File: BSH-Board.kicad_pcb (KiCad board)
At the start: 2 copper layers, 20 x 30 mm, 47 parts, among them J1 667101210103, J2 MICRO QTZB5.0, SW1 TS-3025-B-C-B, SW2 TS-3025-B-C-B, U1 ESP32-C6-MINI-1-N4, U2 AP63203WU, U3 NCP715SQ50T2G, U4 TXS0102DQER

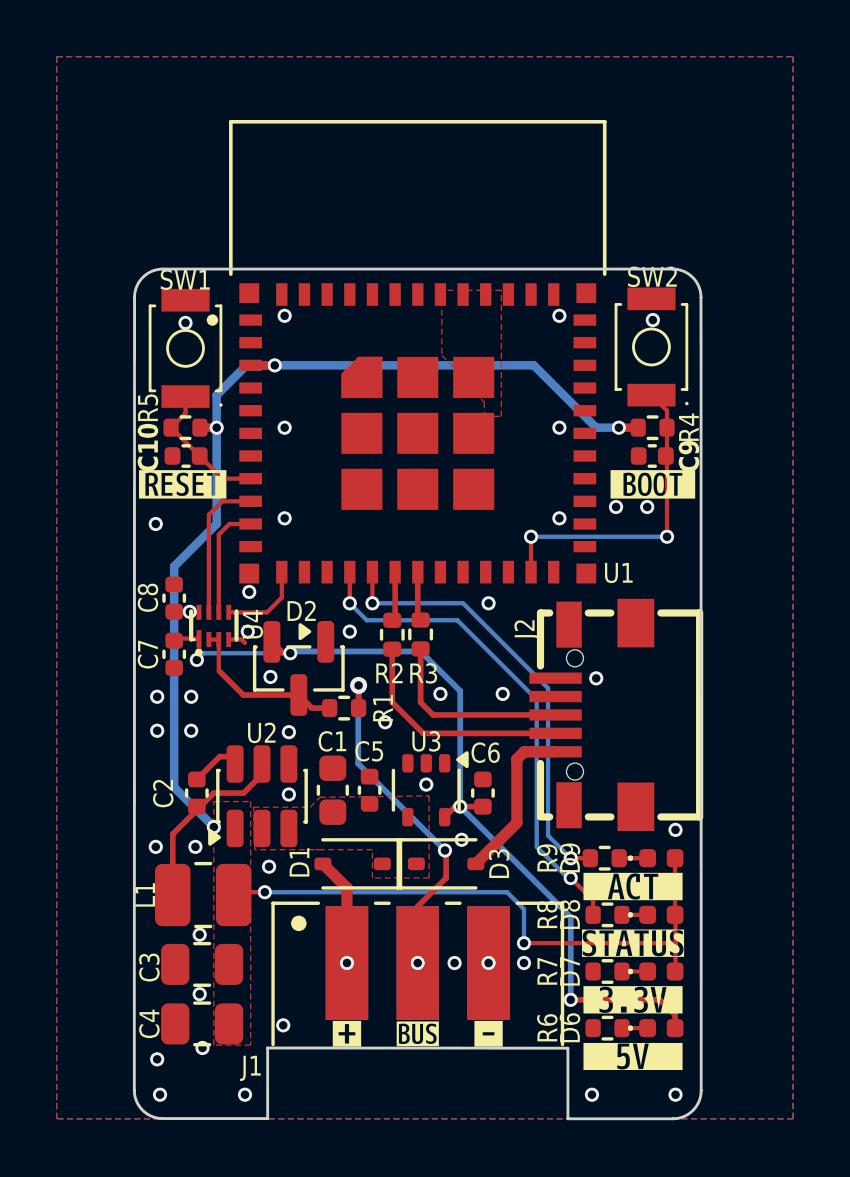
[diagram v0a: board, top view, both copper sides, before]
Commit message: Fix TXS0102DQER bug
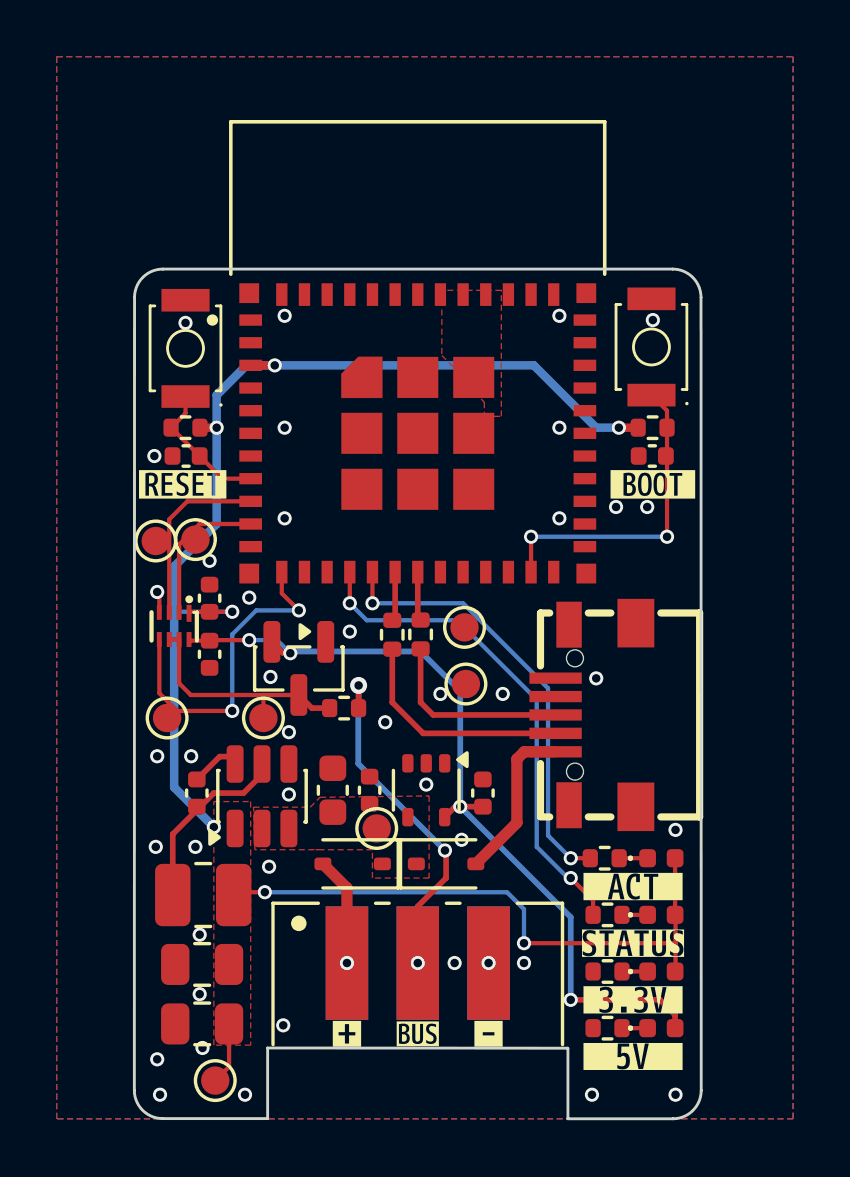
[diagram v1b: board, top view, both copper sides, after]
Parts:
- added TP1: TestPoint, TestPoint:TestPoint_Pad_D1.0mm, F.Cu at (113.2, 76.8)
- added TP2: TestPoint, TestPoint:TestPoint_Pad_D1.0mm, F.Cu at (116.5, 76.8)
- added TP3: TestPoint, TestPoint:TestPoint_Pad_D1.0mm, F.Cu at (114.2, 70.5)
- added TP4: TestPoint, TestPoint:TestPoint_Pad_D1.0mm, F.Cu at (112.8, 70.6)
- added TP5: TestPoint, TestPoint:TestPoint_Pad_D1.0mm, F.Cu at (123.7, 73.7)
- added TP6: TestPoint, TestPoint:TestPoint_Pad_D1.0mm, F.Cu at (120.5, 80.8)
- added TP7: TestPoint, TestPoint:TestPoint_Pad_D1.0mm, F.Cu at (114.8, 89.7)
- added TP8: TestPoint, TestPoint:TestPoint_Pad_D1.0mm, F.Cu at (123.7, 75.7)
- moved U4 1.40 mm to (113.4, 73.6), turned to 180 degrees
- moved C7 1.25 mm to (114.7, 74.6)
- moved C8 1.25 mm to (114.7, 72.6)
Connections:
- U4 pad 1: +5V -> +3.3V
- U4 pad 2: D-BUS -> DBUS-TX
- U4 pad 3: D-BUS -> DBUS-RX
- U4 pad 6: DBUS-TX -> D-BUS
- U4 pad 7: DBUS-RX -> D-BUS
- U4 pad 8: +3.3V -> +5V
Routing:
- net DBUS-ENABLE: track 2.99 -> 11.7 mm, vias 0 -> 2
- net +3.3V: track 56.6 -> 61.0 mm
- net D-BUS: track 5.91 -> 8.38 mm
- net DBUS-RX: track 5.12 -> 6.42 mm
- net +5V: track 30.9 -> 29.6 mm
- net DBUS-TX: track 4.03 -> 5.22 mm
- net GND: track 0.62 -> 0.75 mm, vias 44 -> 42

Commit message: TXS0102 OE directly to 3.3v, all spare IOs to Testpoints
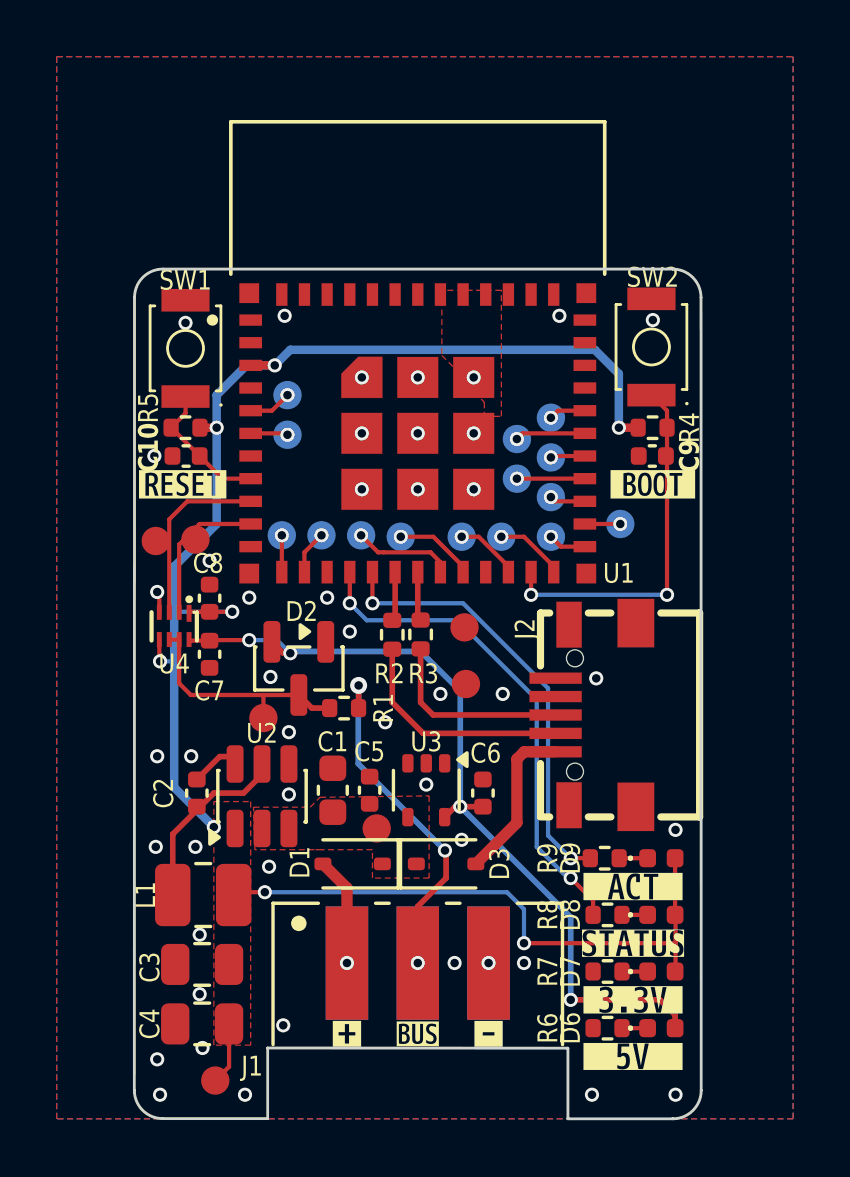
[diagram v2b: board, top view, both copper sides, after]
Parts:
- removed the TP1 at (113.2, 76.8)
- added TP10: TestPoint, Testpoints:TestPoint_Pad_D1.0mm, B.Cu at (117.4, 65.5)
- added TP11: TestPoint, Testpoints:TestPoint_Pad_D1.0mm, B.Cu at (117.4, 66.8)
- added TP12: TestPoint, Testpoints:TestPoint_Pad_D1.0mm, B.Cu at (123.5, 70.5)
- added TP13: TestPoint, Testpoints:TestPoint_Pad_D1.0mm, B.Cu at (120.0, 70.4)
- added TP14: TestPoint, Testpoints:TestPoint_Pad_D1.0mm, B.Cu at (121.4, 70.5)
- added TP15: TestPoint, Testpoints:TestPoint_Pad_D1.0mm, B.Cu at (125.0, 70.5)
- added TP16: TestPoint, Testpoints:TestPoint_Pad_D1.0mm, B.Cu at (126.7, 70.5)
- added TP17: TestPoint, Testpoints:TestPoint_Pad_D1.0mm, B.Cu at (129.2, 70.0)
- added TP18: TestPoint, Testpoints:TestPoint_Pad_D1.0mm, B.Cu at (126.7, 69.0)
- added TP19: TestPoint, Testpoints:TestPoint_Pad_D1.0mm, B.Cu at (125.5, 68.4)
- added TP20: TestPoint, Testpoints:TestPoint_Pad_D1.0mm, B.Cu at (126.7, 67.7)
- added TP21: TestPoint, Testpoints:TestPoint_Pad_D1.0mm, B.Cu at (126.7, 66.2)
- added TP22: TestPoint, Testpoints:TestPoint_Pad_D1.0mm, B.Cu at (125.5, 67.0)
- added TP8: TestPoint, Testpoints:TestPoint_Pad_D1.0mm, B.Cu at (117.2, 70.4)
- added TP9: TestPoint, Testpoints:TestPoint_Pad_D1.0mm, B.Cu at (118.6, 70.4)
- R6, R9: value 330 -> 510
- TP1: renamed from TP2; footprint TestPoint:TestPoint_Pad_D1.0mm -> Testpoints:TestPoint_Pad_D1.0mm
- TP2: renamed from TP3; footprint TestPoint:TestPoint_Pad_D1.0mm -> Testpoints:TestPoint_Pad_D1.0mm
- TP3: renamed from TP4; footprint TestPoint:TestPoint_Pad_D1.0mm -> Testpoints:TestPoint_Pad_D1.0mm
- TP4: renamed from TP5; footprint TestPoint:TestPoint_Pad_D1.0mm -> Testpoints:TestPoint_Pad_D1.0mm
- TP5: renamed from TP6; footprint TestPoint:TestPoint_Pad_D1.0mm -> Testpoints:TestPoint_Pad_D1.0mm
- TP6: renamed from TP7; footprint TestPoint:TestPoint_Pad_D1.0mm -> Testpoints:TestPoint_Pad_D1.0mm
- TP7: renamed from TP8; footprint TestPoint:TestPoint_Pad_D1.0mm -> Testpoints:TestPoint_Pad_D1.0mm
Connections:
- U1 pad 12: DBUS-ENABLE -> Net-(U1-IO0)
- U1 pad 13: unconnected-(U1-IO1-Pad13) -> Net-(U1-IO1)
- U1 pad 19: unconnected-(U1-IO14-Pad19) -> Net-(U1-IO14)
- U1 pad 20: unconnected-(U1-IO15-Pad20) -> Net-(U1-IO15)
- U1 pad 22: unconnected-(U1-IO8-Pad22) -> Net-(U1-IO8)
- U1 pad 24: unconnected-(U1-IO18-Pad24) -> Net-(U1-IO18)
- U1 pad 25: unconnected-(U1-IO19-Pad25) -> Net-(U1-IO19)
- U1 pad 26: unconnected-(U1-IO20-Pad26) -> Net-(U1-IO20)
- U1 pad 27: unconnected-(U1-IO21-Pad27) -> Net-(U1-IO21)
- U1 pad 28: unconnected-(U1-IO22-Pad28) -> Net-(U1-IO22)
- U1 pad 29: unconnected-(U1-IO23-Pad29) -> Net-(U1-IO23)
- U1 pad 30: unconnected-(U1-RXD0-Pad30) -> Net-(U1-RXD0)
- U1 pad 31: unconnected-(U1-TXD0-Pad31) -> Net-(U1-TXD0)
- U1 pad 5: unconnected-(U1-IO2-Pad5) -> Net-(U1-IO2)
- U1 pad 6: unconnected-(U1-IO3-Pad6) -> Net-(U1-IO3)
- U4 pad 5: DBUS-ENABLE -> +3.3V
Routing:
- net DBUS-ENABLE: track 11.7 -> 0.00 mm, vias 2 -> 0
- net Net-(U1-IO14): track 0.00 -> 3.54 mm, vias 0 -> 1
- net +3.3V: track 61.0 -> 63.9 mm, vias 7 -> 8
- net Net-(U1-IO15): track 0.00 -> 2.83 mm, vias 0 -> 1
- net Net-(U1-IO18): track 0.00 -> 2.48 mm, vias 0 -> 1
- net Net-(U1-RXD0): track 0.00 -> 2.48 mm, vias 0 -> 1
- net Net-(U1-IO22): track 0.00 -> 2.40 mm, vias 0 -> 1
- net Net-(U1-IO8): track 0.00 -> 2.28 mm, vias 0 -> 1
- net BOOT: track 11.3 -> 12.9 mm
- net Net-(U1-IO1): track 0.00 -> 1.55 mm, vias 0 -> 1
- net Net-(U1-IO2): track 0.00 -> 1.53 mm, vias 0 -> 1
- net Net-(U1-IO19): track 0.00 -> 1.34 mm, vias 0 -> 1
- net Net-(U1-IO3): track 0.00 -> 1.32 mm, vias 0 -> 1
- net Net-(U1-TXD0): track 0.00 -> 1.30 mm, vias 0 -> 1
- net Net-(U1-IO0): track 0.00 -> 1.30 mm, vias 0 -> 1
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
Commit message: Removed bottom pads of RAST connector
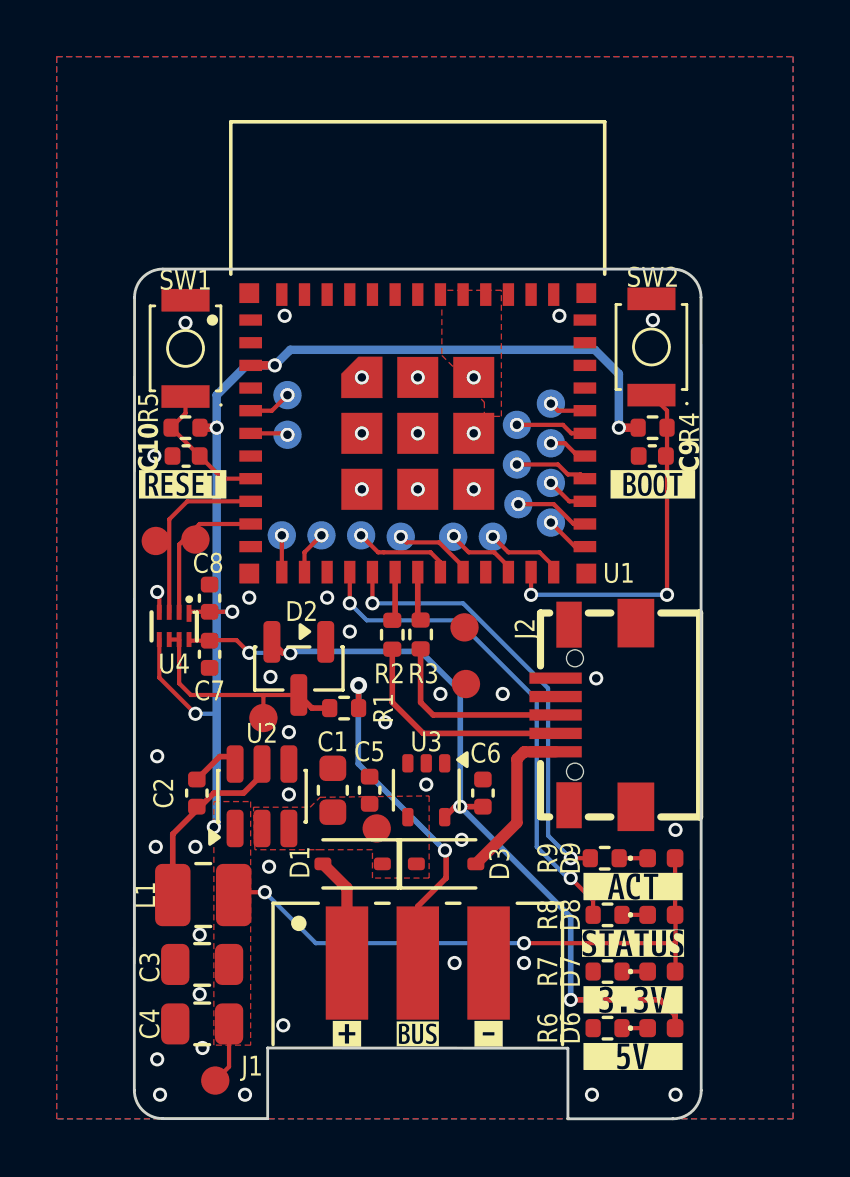
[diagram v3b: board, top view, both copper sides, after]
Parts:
- moved TP17 3.67 mm to (125.5, 69.3)
- moved TP16 0.50 mm to (126.7, 70.0)
- moved TP18 0.50 mm to (126.7, 68.5)
- moved TP19 0.50 mm to (125.5, 67.9)
- moved TP20 0.50 mm to (126.7, 67.2)
- moved TP21 0.50 mm to (126.7, 65.8)
- moved TP22 0.50 mm to (125.5, 66.5)
- moved TP12 0.30 mm to (123.2, 70.5)
- moved TP15 0.30 mm to (124.7, 70.5)
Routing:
- net Net-(U1-IO20): track 1.25 -> 2.64 mm
- net +3.3V: track 63.9 -> 63.1 mm
- net Net-(J1-PadA2): vias 3 -> 2
- net Net-(D1-A): vias 1 -> 0
- net GND: vias 46 -> 43
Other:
- board text added: "00"
- board text added: "01"
- board text added: "02"
- board text added: "03"
- board text added: "08"
- board text added: "14"
- board text added: "15"
- board text added: "18"
- board text added: "19"
- board text added: "20"
- board text added: "21"
- board text added: "22"
- board text added: "23"
- board text added: "RXD0"
- board text added: "TXD0"

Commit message: Replaced TXS0102 with Pullup + 74LVC1G07 + Zener
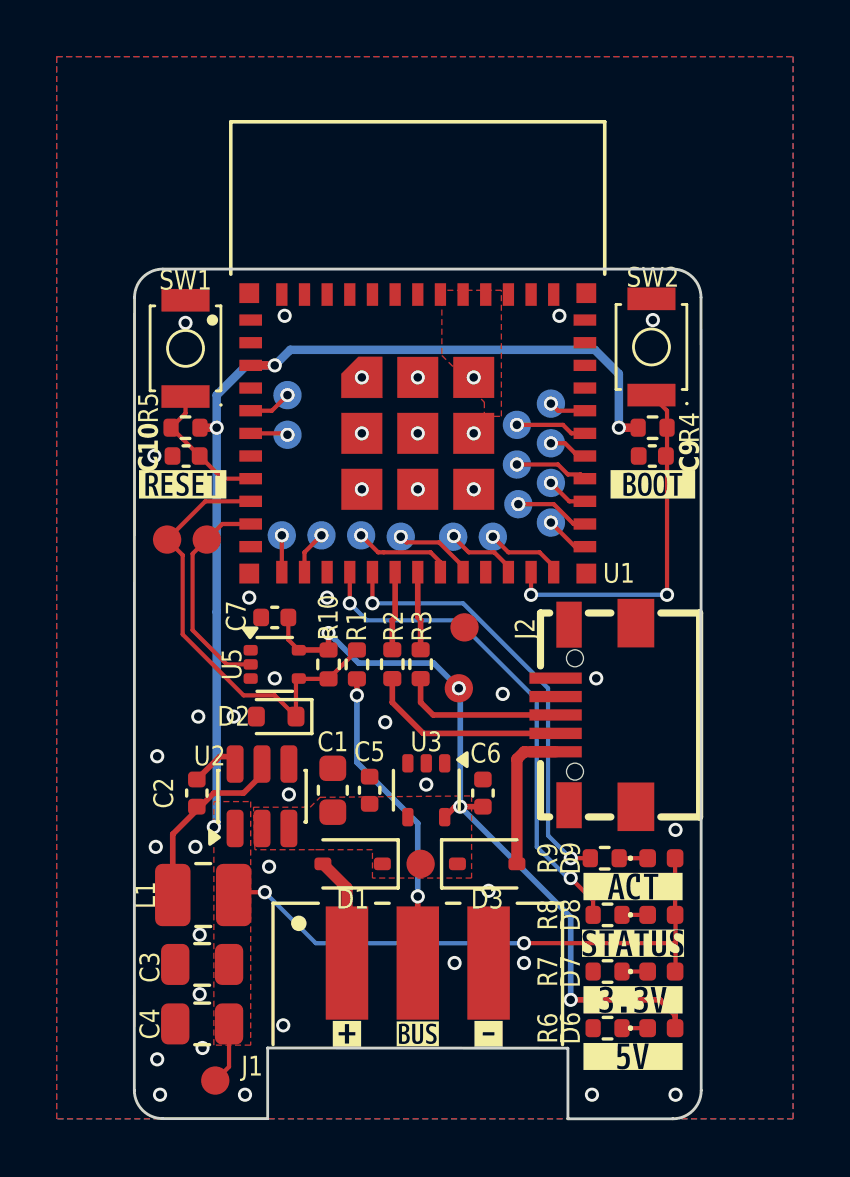
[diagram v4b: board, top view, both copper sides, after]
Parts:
- removed C8: 100nF, Capacitor_SMD:C_0402_1005Metric
- removed the TP1 at (116.5, 76.8)
- removed U4: TXS0102DQER, footprints:X2SON-8_L1.4-W1.0-P0.35-BL
- added R10: 10k, Resistor_SMD:R_0402_1005Metric, F.Cu at (118.8, 75.0)
- added U5: 74LVC1G07, Package_TO_SOT_SMD:Diodes_SOT-553, F.Cu at (117.0, 75.0)
- D2: value BAV99,215 -> BZX584C5V1; footprint Package_TO_SOT_SMD:SOT-23 -> Diode_SMD:D_SOD-523
- R1: value 120 -> 330
- moved C7 2.64 mm to (117.0, 73.3), turned to 0 degrees
- moved TP4 1.99 mm to (122.1, 82.0)
- moved D2 1.88 mm to (117.0, 76.8), turned to 180 degrees
- moved R1 1.61 mm to (119.8, 75.0), turned to 90 degrees
- moved D3 1.45 mm to (124.5, 82.0)
- moved R3 1.05 mm to (122.1, 75.0)
- moved R2 1.04 mm to (121.1, 75.0)
- moved TP2 0.40 mm to (113.2, 70.5)
- moved TP1 0.40 mm to (114.5, 70.5)
- moved TP6 0.29 mm to (123.5, 75.8)
- renumbered TP2 to TP1, TP3 to TP2, TP4 to TP3, TP5 to TP4, TP6 to TP5, TP7 to TP6
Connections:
- net Net-(J1-PadA2) renamed /DBUS
- C7 pad 1: +5V -> GND
- C7 pad 2: GND -> +5V
- D2 pad 1: GND -> DBUS-RX
- D2 pad 2: +5V -> GND
- R1 pad 2: D-BUS -> DBUS-RX
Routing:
- net DBUS-RX: track 6.42 -> 16.2 mm
- net D-BUS: track 8.38 -> 0.00 mm
- net +3.3V: track 63.1 -> 57.1 mm, vias 8 -> 6
- net +5V: track 29.6 -> 26.9 mm
- net DBUS-TX: track 5.22 -> 7.74 mm
- net /DBUS: track 12.3 -> 10.9 mm
- net USB-D+: track 6.84 -> 5.79 mm
- net Net-(U1-IO13): track 1.73 -> 2.78 mm
- net USB-D-: track 8.10 -> 7.06 mm
- net Net-(U1-IO12): track 1.74 -> 2.78 mm
- net GND: track 0.75 -> 0.00 mm, vias 43 -> 41
- net Net-(D3-A): track 5.77 -> 5.17 mm

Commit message: Went back to LSF0102
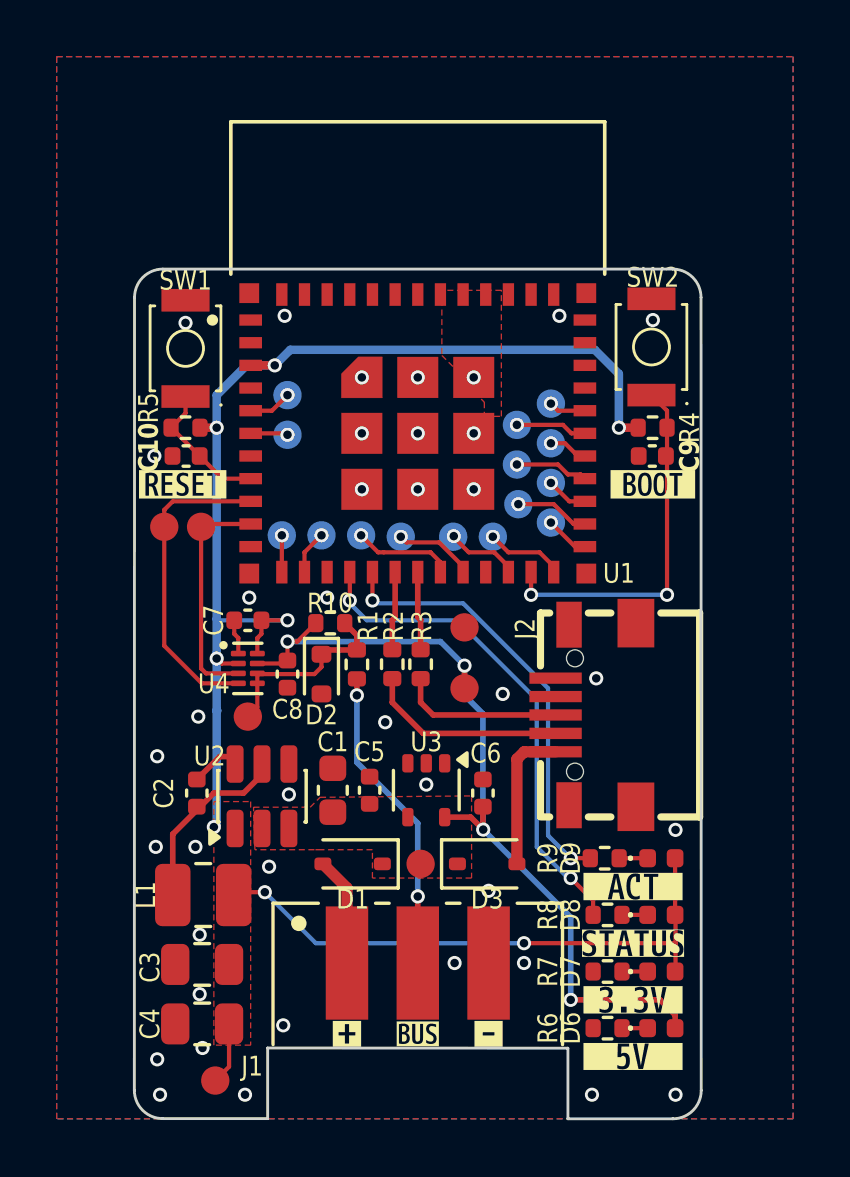
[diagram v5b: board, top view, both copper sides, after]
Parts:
- removed U5: 74LVC1G07, Package_TO_SOT_SMD:Diodes_SOT-553
- added C8: 100nF, Capacitor_SMD:C_0402_1005Metric, F.Cu at (117.4, 75.3)
- added TP2: TestPoint, Testpoints:TestPoint_Pad_D1.0mm, F.Cu at (113.0, 70.1)
- added U4: LSF0102DQER, Package_SON:X2SON-8_1.4x1mm_P0.35mm, F.Cu at (116.0, 75.1)
- D2: value BZX584C5V1 -> BZX584C5V6
- moved TP3 6.87 mm to (116.0, 76.8)
- moved D2 2.19 mm to (118.6, 75.3), turned to -90 degrees
- moved R10 1.46 mm to (118.9, 73.5), turned to 180 degrees
- moved C7 0.96 mm to (116.0, 73.4)
- moved TP1 0.49 mm to (114.3, 70.1)
- moved TP7 0.20 mm to (123.7, 75.8)
- renumbered TP2 to TP3, TP3 to TP4, TP4 to TP5, TP5 to TP6, TP6 to TP7
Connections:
- C7 pad 2: +5V -> +3.3V
- D2 pad 1: DBUS-RX -> Net-(D2-K)
- R1 pad 2: DBUS-RX -> Net-(D2-K)
- R10 pad 1: DBUS-RX -> Net-(D2-K)
- TP1 pad 1: DBUS-TX -> DBUS-RX
- TP3 pad 1: DBUS-RX -> Net-(D2-K)
- U1 pad 10: DBUS-TX -> DBUS-RX
- U1 pad 9: DBUS-RX -> DBUS-TX
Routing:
- net DBUS-RX: track 16.2 -> 8.20 mm
- net Net-(D2-K): track 0.00 -> 6.93 mm
- net +3.3V: track 57.1 -> 62.6 mm, vias 6 -> 8
- net +5V: track 26.9 -> 30.5 mm
- net DBUS-TX: track 7.74 -> 11.1 mm
- net GND: track 0.00 -> 1.24 mm, vias 41 -> 39
